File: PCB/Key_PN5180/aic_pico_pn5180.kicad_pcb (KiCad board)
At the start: 2 copper layers, 50 x 50 mm, 34 parts, among them J1 Conn_01x02_Female, J2 PN5180, SW1 SKRR_4pin, SW10 SKRR_4pin, SW11 SKRR_4pin, SW12 SKRR_4pin, SW2 SKRR_4pin, SW3 SKRR_4pin, SW4 SKRR_4pin, SW5 SKRR_4pin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

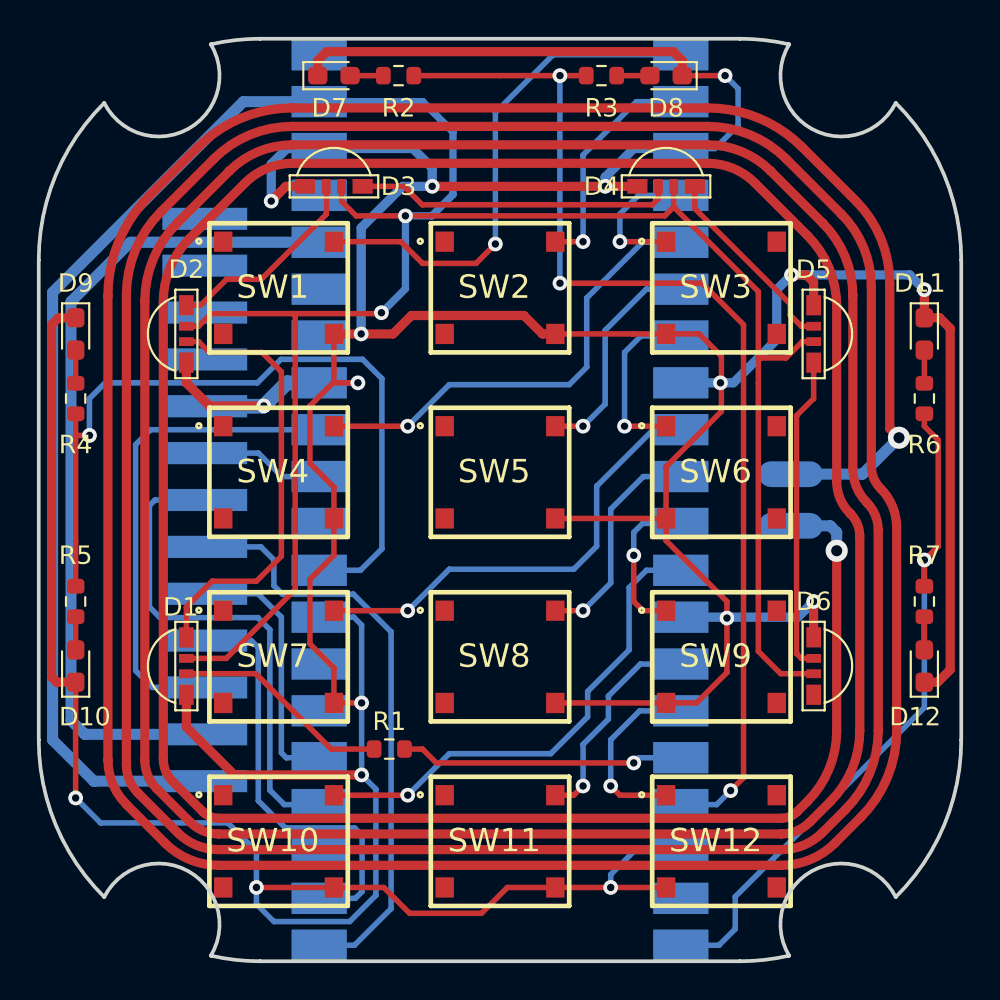
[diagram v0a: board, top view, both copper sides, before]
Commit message: PCB v1.1, pad optimization
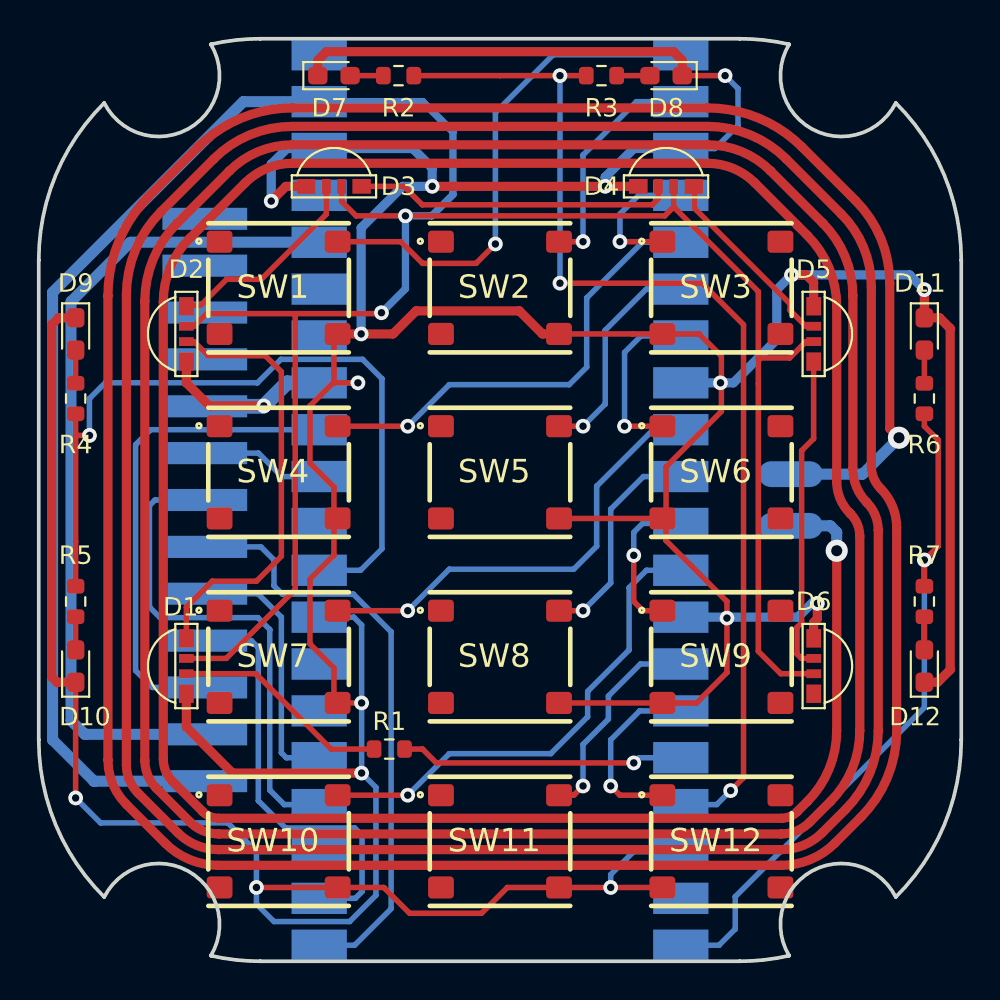
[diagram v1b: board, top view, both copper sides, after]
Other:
- board text added: "AIC Key v1.1"
- board text removed: "AIC Key v1.0"

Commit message: Optimize LED 1204 footprint
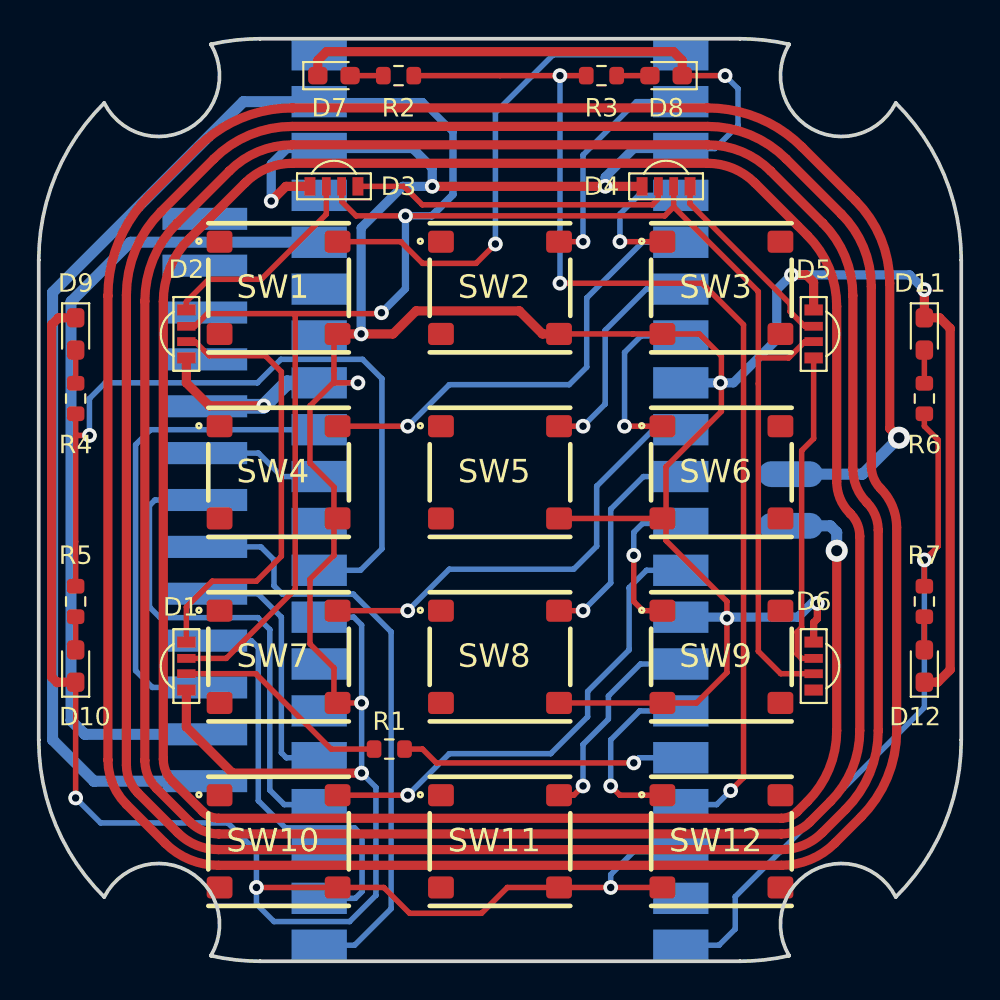
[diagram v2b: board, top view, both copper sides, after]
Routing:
- net GND: track 334.3 -> 335.8 mm
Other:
- board text added: "AIC Key v1.2"
- board text added: "PN5180"
- board text removed: "AIC Key v1.1"
